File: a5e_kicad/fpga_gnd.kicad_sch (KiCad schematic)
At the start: 1 part, among them U1 A5EB013B-B23B

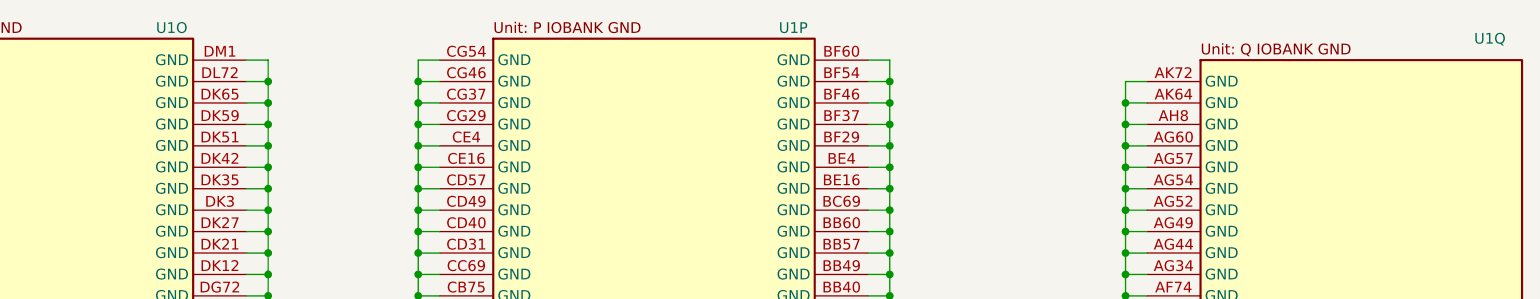
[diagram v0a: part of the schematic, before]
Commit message: add vias to lppdr balls
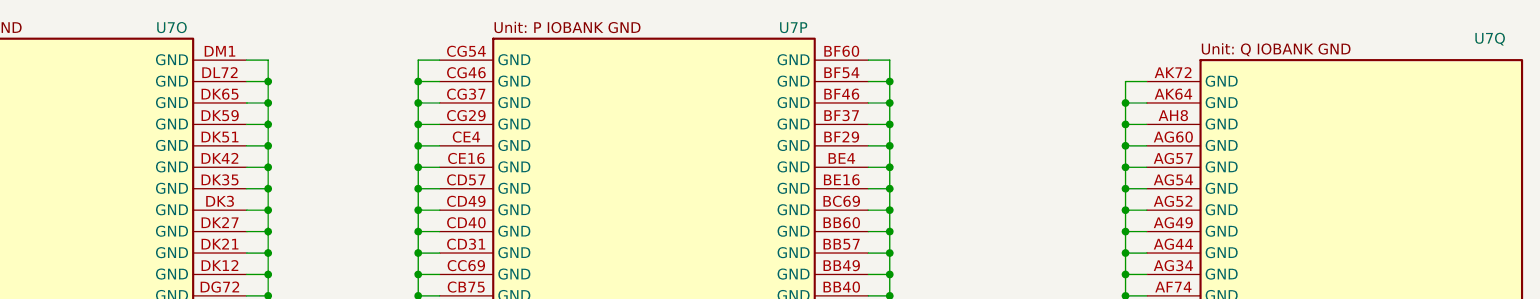
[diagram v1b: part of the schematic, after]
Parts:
- renumbered U1 to U7
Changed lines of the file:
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@@
 		(in_pos_files yes)
 		(dnp no)
-		(property "Reference" "U1"
+		(property "Reference" "U7"
 			(at 228.6 20.32 0)
 			(show_name no)
@@
 			(project "agilex_3_soc"
 				(path "/a5b98d95-6877-4284-904f-d04e32723ae0/7bb42d88-bf35-48aa-a7c0-a9a33c7f84fa"
-					(reference "U1")
+					(reference "U7")
 					(unit 17)
 				)
@@
 		(dnp no)
 		(fields_autoplaced yes)
-		(property "Reference" "#PWR0904"
+		(property "Reference" "#PWR0225"
 			(at 83.82 161.29 0)
 			(hide yes)
@@
 			(project "agilex_3_soc"
 				(path "/a5b98d95-6877-4284-904f-d04e32723ae0/7bb42d88-bf35-48aa-a7c0-a9a33c7f84fa"
-					(reference "#PWR0904")
+					(reference "#PWR0225")
 					(unit 1)
 				)
@@
 		(dnp no)
 		(fields_autoplaced yes)
-		(property "Reference" "#PWR0902"
+		(property "Reference" "#PWR0226"
 			(at 101.6 161.29 0)
 			(hide yes)
@@
 			(project "agilex_3_soc"
 				(path "/a5b98d95-6877-4284-904f-d04e32723ae0/7bb42d88-bf35-48aa-a7c0-a9a33c7f84fa"
-					(reference "#PWR0902")
+					(reference "#PWR0226")
 					(unit 1)
 				)
@@
 		(dnp no)
 		(fields_autoplaced yes)
-		(property "Reference" "#PWR0901"
+		(property "Reference" "#PWR0224"
 			(at 27.94 161.29 0)
 			(hide yes)
@@
 			(project "agilex_3_soc"
 				(path "/a5b98d95-6877-4284-904f-d04e32723ae0/7bb42d88-bf35-48aa-a7c0-a9a33c7f84fa"
-					(reference "#PWR0901")
+					(reference "#PWR0224")
 					(unit 1)
 				)
@@
 		(in_pos_files yes)
 		(dnp no)
-		(property "Reference" "U1"
+		(property "Reference" "U7"
 			(at 72.39 19.05 0)
 			(show_name no)
@@
 			(project "agilex_3_soc"
 				(path "/a5b98d95-6877-4284-904f-d04e32723ae0/7bb42d88-bf35-48aa-a7c0-a9a33c7f84fa"
-					(reference "U1")
+					(reference "U7")
 					(unit 15)
 				)
@@
 		(dnp no)
 		(fields_autoplaced yes)
-		(property "Reference" "#PWR0905"
+		(property "Reference" "#PWR0228"
 			(at 185.42 115.57 0)
 			(hide yes)
@@
 			(project "agilex_3_soc"
 				(path "/a5b98d95-6877-4284-904f-d04e32723ae0/7bb42d88-bf35-48aa-a7c0-a9a33c7f84fa"
-					(reference "#PWR0905")
+					(reference "#PWR0228")
 					(unit 1)
 				)
@@
 		(dnp no)
 		(fields_autoplaced yes)
-		(property "Reference" "#PWR0903"
+		(property "Reference" "#PWR0227"
 			(at 157.48 161.29 0)
 			(hide yes)
@@
 			(project "agilex_3_soc"
 				(path "/a5b98d95-6877-4284-904f-d04e32723ae0/7bb42d88-bf35-48aa-a7c0-a9a33c7f84fa"
-					(reference "#PWR0903")
+					(reference "#PWR0227")
 					(unit 1)
 				)
@@
 		(in_pos_files yes)
 		(dnp no)
-		(property "Reference" "U1"
+		(property "Reference" "U7"
 			(at 146.05 19.05 0)
 			(show_name no)
@@
 			(project "agilex_3_soc"
 				(path "/a5b98d95-6877-4284-904f-d04e32723ae0/7bb42d88-bf35-48aa-a7c0-a9a33c7f84fa"
-					(reference "U1")
+					(reference "U7")
 					(unit 16)
 				)
